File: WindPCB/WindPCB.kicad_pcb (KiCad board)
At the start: 2 copper layers, 63.5 x 45 mm, 32 parts, among them J6 Conn_01x04, U2 TSR_1-2450, U3 SeeeduinoXIAO, U4 MCP2562-E-P, U5 TSR1-2433E, U6 LM7806_TO220

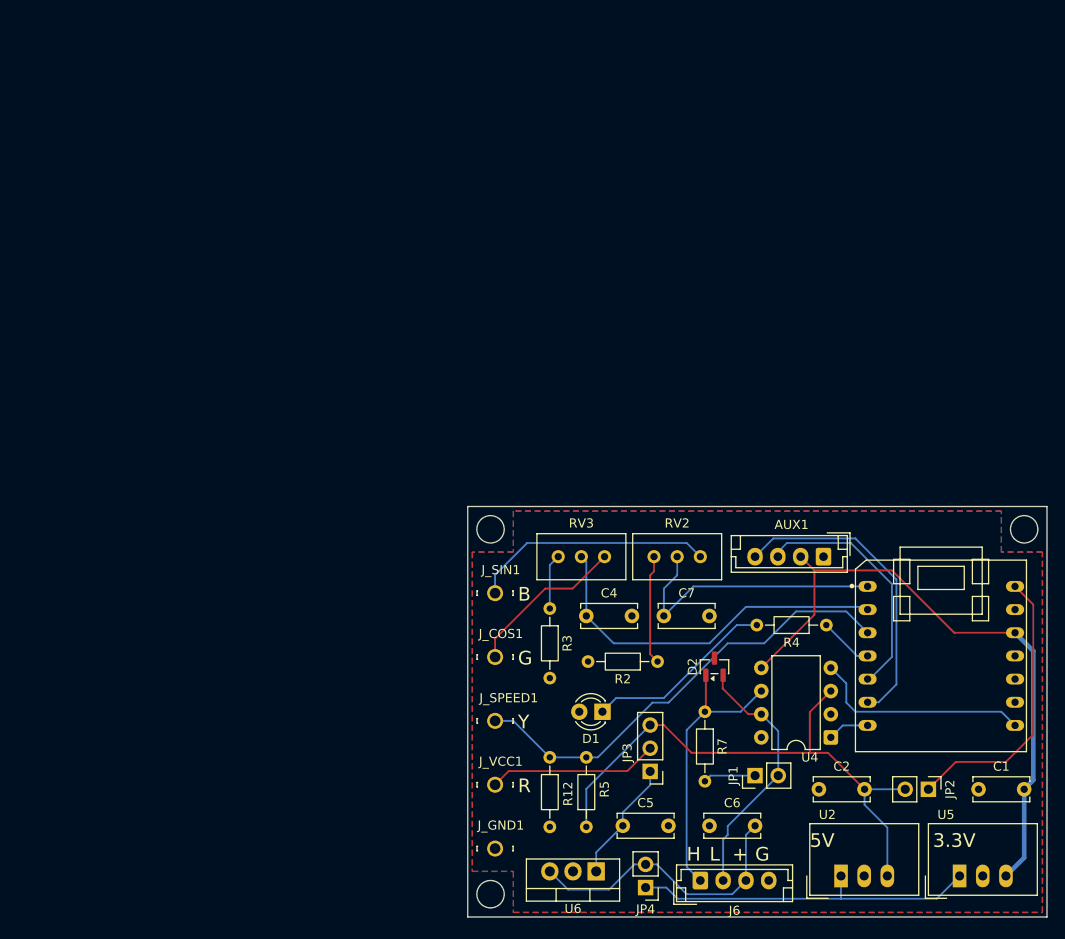
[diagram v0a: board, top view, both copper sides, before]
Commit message: Work in progress: use a MCP3202 instead of the the ESP32 ADC
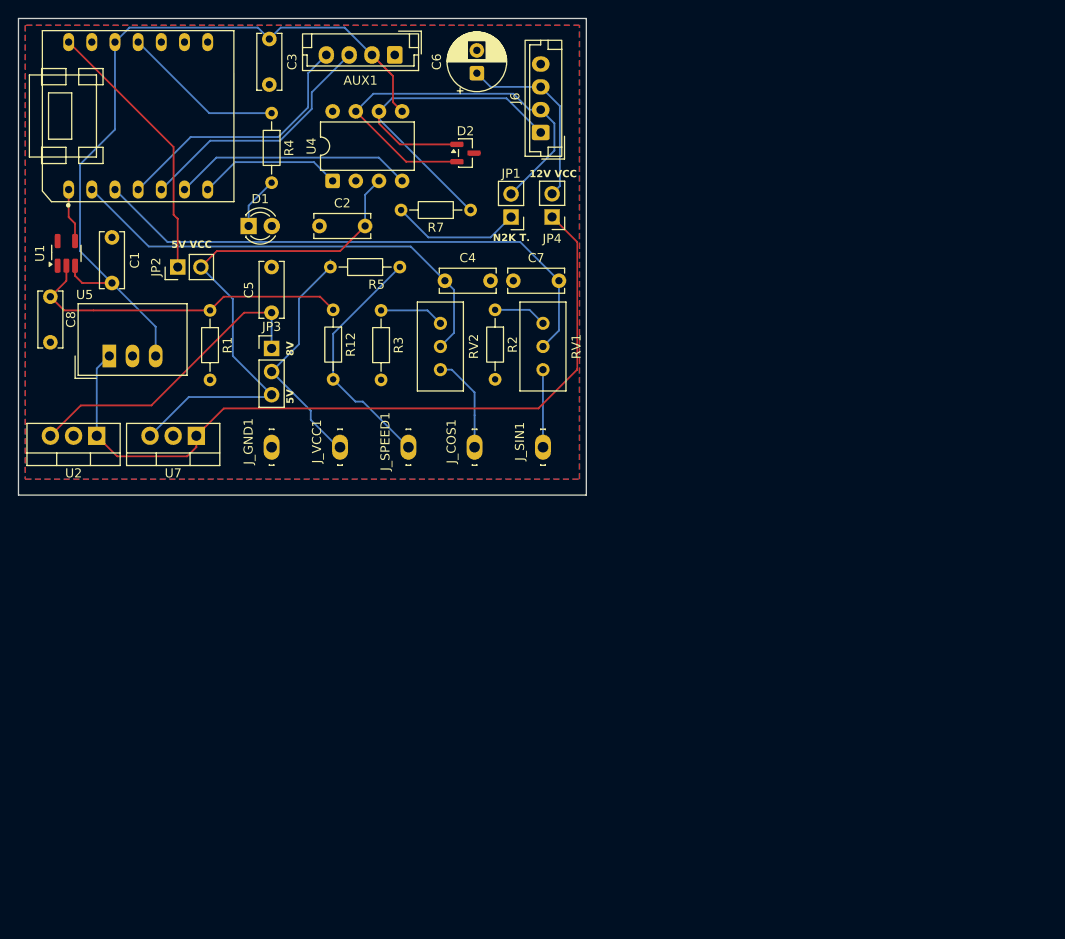
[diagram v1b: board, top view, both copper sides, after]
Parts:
- removed RV3: 5K, Potentiometer_THT:Potentiometer_Bourns_3296W_Vertical
- removed U6: LM7806_TO220, Package_TO_SOT_THT:TO-220-3_Vertical
- added C3: 100nF, Capacitor_THT:C_Disc_D6.0mm_W2.5mm_P5.00mm, F.Cu at (47.2, 15.2)
- added C8: 47nF, Capacitor_THT:C_Disc_D6.0mm_W2.5mm_P5.00mm, F.Cu at (23.2, 43.5)
- added R1: 4K7, Resistor_THT:R_Axial_DIN0204_L3.6mm_D1.6mm_P7.62mm_Horizontal, F.Cu at (40.8, 45.0)
- added RV1: 5K, Potentiometer_THT:Potentiometer_Bourns_3296W_Vertical, F.Cu at (77.2, 51.5)
- added U1: 74AHC1G14, Package_TO_SOT_SMD:SOT-23-5_HandSoldering, F.Cu at (25.0, 38.8)
- added U7: LM7805_TO220, Package_TO_SOT_THT:TO-220-3_Vertical, F.Cu at (39.2, 58.8)
- C4, C7: value 1nF -> 22nF
- C6: value 330nF -> 330uF; footprint Capacitor_THT:C_Disc_D6.0mm_W2.5mm_P5.00mm -> Capacitor_THT:CP_Radial_D6.3mm_P2.50mm
- R12: value 3K3 -> 2K2
- R2, R3: value 2K -> 3K3
- R5: value 2K2 -> 4K7
- U2: value TSR_1-2450 -> LM7808_TO220; footprint Converter_DCDC:Converter_DCDC_TRACO_TSR-1_THT -> Package_TO_SOT_THT:TO-220-3_Vertical
- moved C1 112.6 mm to (30.0, 37.0), turned to -90 degrees
- moved U5 109.3 mm to (29.7, 50.0)
- moved JP2 100.2 mm to (37.2, 40.2), turned to 90 degrees
- moved U2 94.8 mm to (28.3, 58.8), turned to 180 degrees
- moved U3 91.7 mm to (43.4, 32.6), turned to 90 degrees
- moved C6 88.0 mm to (70.0, 19.0), turned to 90 degrees
- moved J6 83.8 mm to (77.0, 25.5), turned to 90 degrees
- moved R4 82.7 mm to (47.5, 23.4), turned to -90 degrees
- moved U4 81.9 mm to (54.2, 30.8), turned to 90 degrees
- moved C2 79.3 mm to (57.8, 35.8), turned to 180 degrees
- moved JP4 74.2 mm to (78.2, 34.8)
- moved AUX1 72.3 mm to (61.0, 17.0)
- moved C5 71.1 mm to (47.5, 45.2), turned to 90 degrees
- moved JP1 66.8 mm to (73.8, 34.8), turned to 180 degrees
- moved D1 65.9 mm to (45.0, 35.8), turned to 0 degrees
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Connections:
- C2 pad 1: GND -> +5V
- C2 pad 2: +5V -> GND
- C5 pad 1: GND -> +8V
- C5 pad 2: +6V -> GND
- C7 pad 1: Net-(U3-PA02_A0_D0) -> Net-(U3-PA10_A2_D2)
- JP3 pad 1: +6V -> +8V
- J_SPEED1 pad 1: Net-(U3-PA10_A2_D2) -> Net-(J_SPEED1-Pad1)
- R12 pad 1: Net-(U3-PA10_A2_D2) -> Net-(C8-Pad1)
- R12 pad 2: GND -> Net-(J_SPEED1-Pad1)
- R4 pad 1: Net-(U3-PA11_A3_D3) -> Net-(U3-PA6_A10_D10_MOSI)
- R5 pad 1: +5V -> Net-(J_SPEED1-Pad1)
- R5 pad 2: Net-(U3-PA10_A2_D2) -> Net-(JP3-C)
- RV2 pad 1: Net-(J_SIN1-Pad1) -> Net-(J_COS1-Pad1)
- RV2 pad 2: Net-(U3-PA02_A0_D0) -> Net-(U3-PA4_A1_D1)
- RV2 pad 3: Net-(R2-Pad1) -> Net-(R3-Pad1)
- U2 pad 3: +5V -> +8V
- U3 pad 11: unconnected-(U3-PA6_A10_D10_MOSI-Pad11) -> Net-(U3-PA6_A10_D10_MOSI)
- U3 pad 4: Net-(U3-PA11_A3_D3) -> Net-(AUX1-Pin_4)
- U3 pad 6: Net-(AUX1-Pin_4) -> Net-(U3-PA9_A5_D5_SCL)
- U3 pad 8: Net-(U3-PB09_A7_D7_RX) -> unconnected-(U3-PB09_A7_D7_RX-Pad8)
- U4 pad 4: Net-(U3-PB09_A7_D7_RX) -> Net-(U3-PA9_A5_D5_SCL)
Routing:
- net Net-(JP4-A): track 38.5 -> 85.5 mm
- net Net-(C8-Pad1): track 0.00 -> 37.0 mm
- net +8V: track 0.00 -> 33.8 mm
- net Net-(J_SPEED1-Pad1): track 0.00 -> 26.7 mm
- net Net-(U3-PA9_A5_D5_SCL): track 0.00 -> 26.4 mm
- net Net-(U3-PA02_A0_D0): track 30.8 -> 5.94 mm
- net Net-(U3-PB09_A7_D7_RX): track 24.0 -> 0.00 mm
- net Net-(J6-Pin_2): track 28.3 -> 47.0 mm
- net Net-(J_SIN1-Pad1): track 26.6 -> 8.50 mm
- net Net-(U3-PA6_A10_D10_MOSI): track 0.00 -> 18.0 mm
- net Net-(D1-K): track 20.9 -> 5.79 mm
- net +3.3V: track 68.8 -> 83.6 mm
- net Net-(J6-Pin_1): track 31.1 -> 45.7 mm
- net +6V: track 13.4 -> 0.00 mm
- net +12V: track 31.9 -> 20.6 mm
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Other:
- board size 63.5 x 45 mm -> 62.2 x 52.2 mm
- board text added: "12V VCC"
- board text added: "5V VCC"
- board text added: "8V"
- board text added: "N2K T."
- board text removed: "+"
- board text removed: "3.3V"
- board text removed: "B"
- board text removed: "G"
- board text removed: "H"
- board text removed: "L"
- board text removed: "R"
- board text removed: "Y"
